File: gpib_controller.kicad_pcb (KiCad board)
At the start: 2 copper layers, 82.7 x 65.1 mm, 43 parts, among them J1 112-024-113R001, J2 FTSH-105-01-L-DV-K, J3 RJHSE5380, J4 USB4085-GF-A, U1 SN74LVC8T245PWR, U2 SN74LVC07APWR, U3 STM32H533RETx, U4 PTS645SH43SMTR92 LFS, U5 THVD1451D, U6 SN74LVC1G07DCKR, U7 SN74LVC14APWR, U8 USBLC6-2SC6, U9 TPSM861253RDXR, Y1 MU00525-32.768K, Y2 CS10820-24M

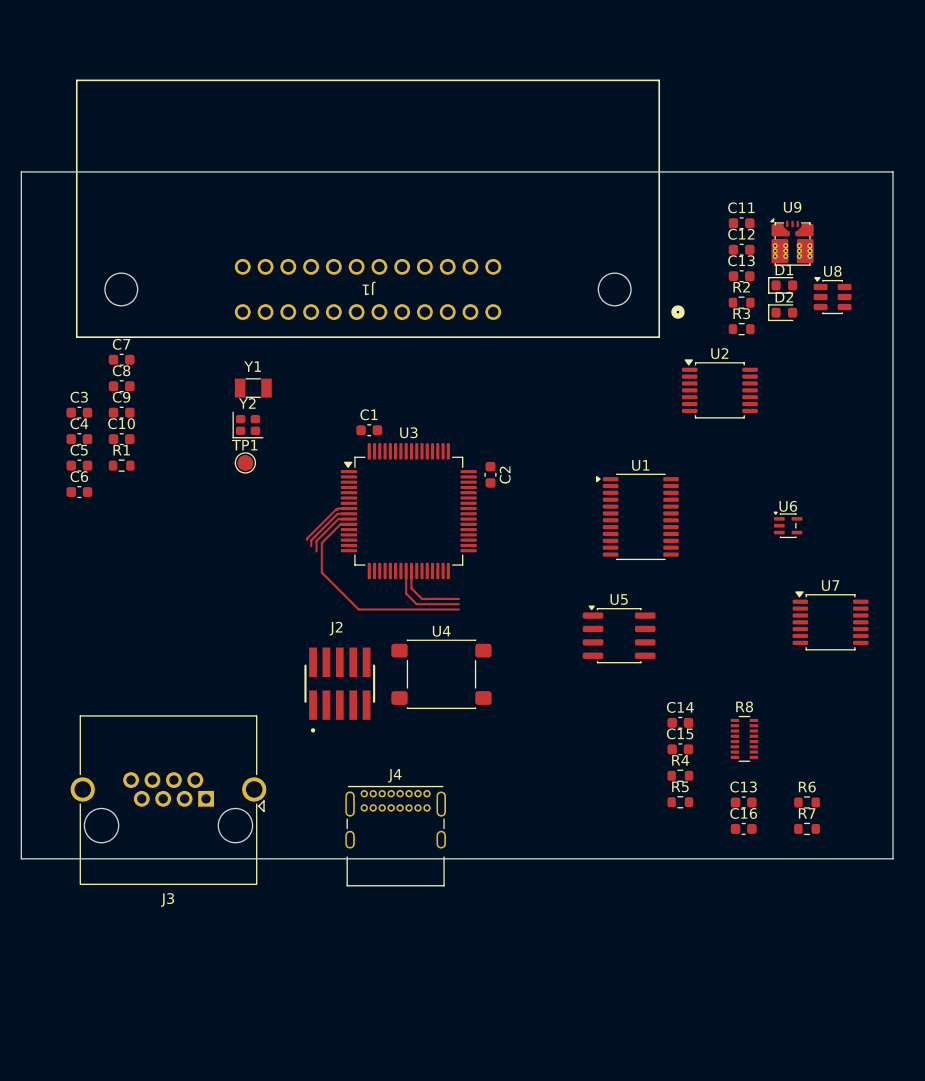
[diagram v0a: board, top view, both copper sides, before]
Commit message: Fix GPIB DIO bus nets and start PCB. Adjusted to 4 layers
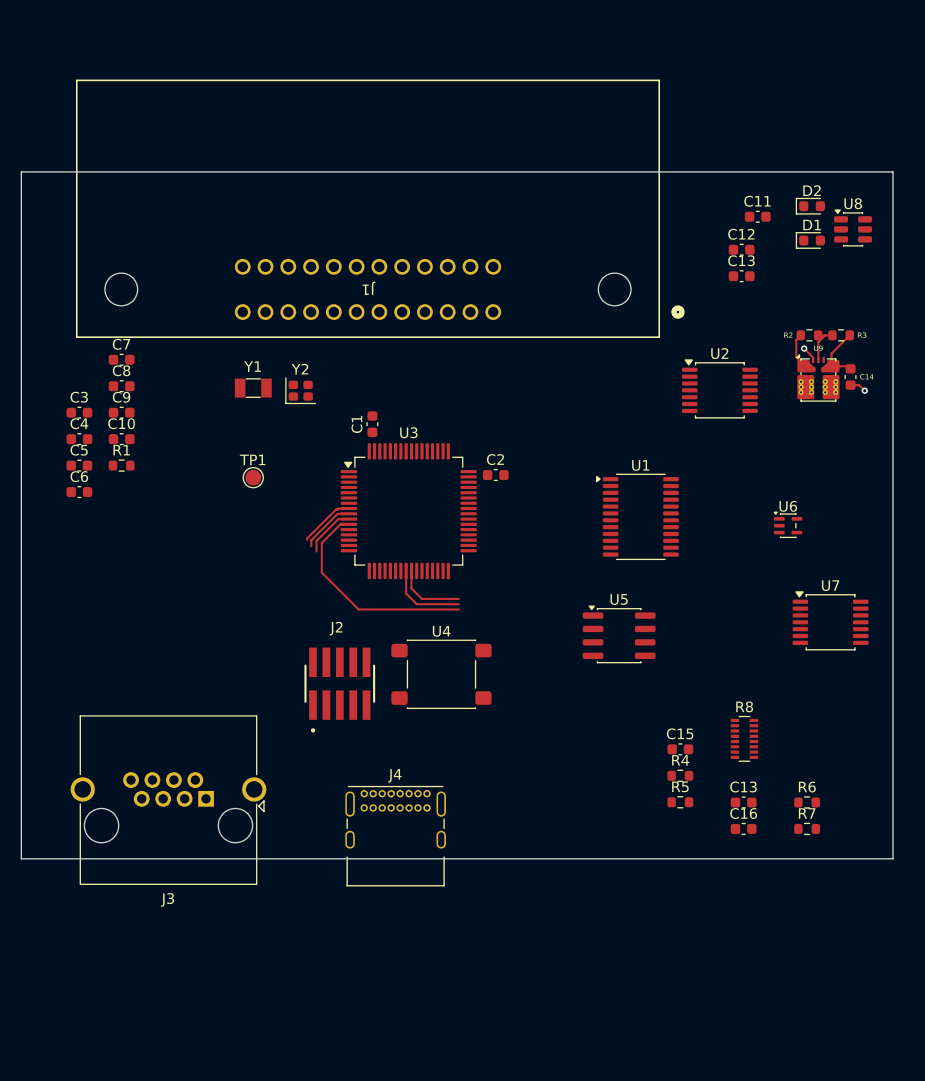
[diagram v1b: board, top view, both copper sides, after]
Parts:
- moved C14 36.6 mm to (212.2, 87.5), turned to 90 degrees
- moved U9 13.1 mm to (209.1, 87.7)
- moved D2 10.4 mm to (208.5, 71.2)
- moved R3 9.45 mm to (211.2, 83.5)
- moved R2 7.14 mm to (208.2, 83.5)
- moved U8 6.70 mm to (212.4, 73.5)
- moved Y2 5.96 mm to (160.0, 88.8)
- moved D1 5.01 mm to (208.5, 74.5)
- moved C11 1.65 mm to (203.3, 72.2)
- moved TP1 1.59 mm to (155.5, 97.0)
- moved C1 0.65 mm to (166.8, 91.9), turned to 90 degrees
- moved C2 0.50 mm to (178.5, 96.8), turned to 0 degrees
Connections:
- J1 pad 10: /Overview/Connectors/ATN -> /Overview/Connectors/SRQ
- J1 pad 17: /Overview/Connectors/ATN -> /Overview/Connectors/REN
- J1 pad 5: /Overview/Connectors/ATN -> /Overview/Connectors/EOI
- J1 pad 6: /Overview/Connectors/ATN -> /Overview/Connectors/DAV
- J1 pad 7: /Overview/Connectors/ATN -> /Overview/Connectors/NRFD
- J1 pad 8: /Overview/Connectors/ATN -> /Overview/Connectors/NDAC
- J1 pad 9: /Overview/Connectors/ATN -> /Overview/Connectors/IFC
- R8 pad 1: /Overview/Connectors/ATN -> /Overview/Connectors/DAV
- R8 pad 2: /Overview/Connectors/ATN -> /Overview/Connectors/NRFD
- R8 pad 3: /Overview/Connectors/ATN -> /Overview/Connectors/NDAC
- R8 pad 5: /Overview/Connectors/ATN -> /Overview/Connectors/IFC
- R8 pad 6: /Overview/Connectors/ATN -> /Overview/Connectors/EOI
- R8 pad 7: /Overview/Connectors/ATN -> /Overview/Connectors/REN
- R8 pad 8: /Overview/Connectors/ATN -> /Overview/Connectors/SRQ
- U1 pad 14: /Overview/GPIB Transceiver/DIO8 -> /Overview/Connectors/DIO8
- U2 pad 10: /Overview/Connectors/ATN -> /Overview/Connectors/IFC
- U2 pad 12: /Overview/Connectors/ATN -> /Overview/Connectors/EOI
- U2 pad 2: /Overview/Connectors/ATN -> /Overview/Connectors/DAV
- U2 pad 4: /Overview/Connectors/ATN -> /Overview/Connectors/NRFD
- U2 pad 6: /Overview/Connectors/ATN -> /Overview/Connectors/NDAC
- U3 pad 38: /Overview/Microcontroller/iDIO8 -> /Overview/GPIB Transceiver/iDIO8
- U6 pad 4: /Overview/Connectors/ATN -> /Overview/Connectors/REN
- U7 pad 1: /Overview/Connectors/ATN -> /Overview/Connectors/SRQ
- U7 pad 11: /Overview/Connectors/ATN -> /Overview/Connectors/DAV
- U7 pad 3: /Overview/Connectors/ATN -> /Overview/Connectors/EOI
- U7 pad 5: /Overview/Connectors/ATN -> /Overview/Connectors/NDAC
- U7 pad 9: /Overview/Connectors/ATN -> /Overview/Connectors/NRFD
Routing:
- net GND: track 0.00 -> 5.55 mm
- net Net-(U9-EN): track 0.00 -> 3.95 mm
- net +5V: track 0.00 -> 3.46 mm
- net +3V3: track 0.00 -> 3.00 mm, vias 0 -> 2
- added copper zone on In1.Cu, net +3V3
- added copper zone on In2.Cu, net GND
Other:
- copper layers 2 -> 4

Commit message: Adjust board size
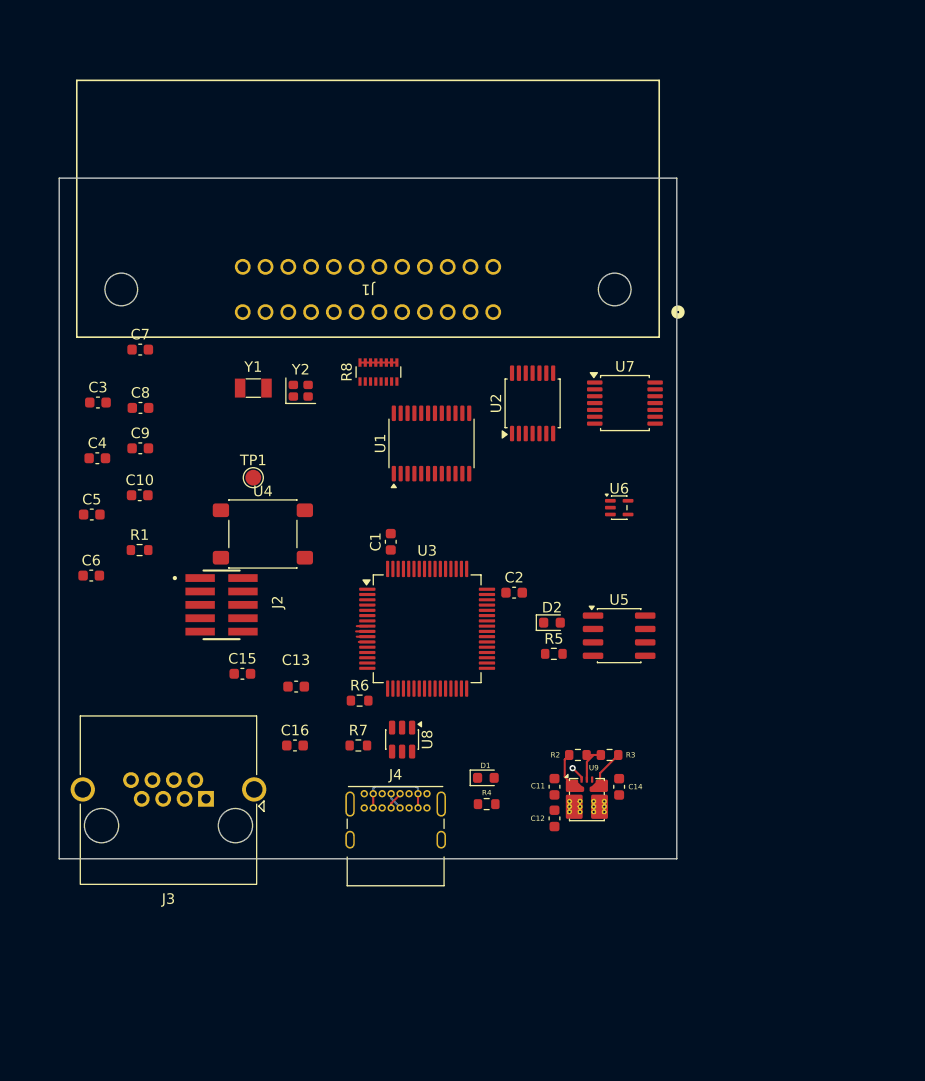
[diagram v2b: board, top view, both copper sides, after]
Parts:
- removed the C13 at (201.8, 77.9)
- moved U8 64.6 mm to (169.6, 121.8), turned to -90 degrees
- moved D1 59.6 mm to (177.6, 125.5)
- moved C11 57.4 mm to (184.1, 126.3), turned to 90 degrees
- moved C12 56.8 mm to (184.1, 129.3), turned to -90 degrees
- moved R8 49.2 mm to (167.4, 87.0), turned to 90 degrees
- moved D2 46.6 mm to (183.8, 110.8)
- moved U9 45.5 mm to (187.1, 127.5)
- moved R2 45.5 mm to (186.3, 123.3)
- moved R3 45.5 mm to (189.3, 123.3)
- moved C14 44.6 mm to (190.2, 126.3)
- moved C13 43.8 mm to (159.6, 116.8)
- moved R6 43.5 mm to (165.6, 118.1)
- moved R7 43.3 mm to (165.5, 122.4)
- moved C16 43.3 mm to (159.5, 122.4)
- moved C15 42.2 mm to (154.5, 115.6)
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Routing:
- net /Overview/GPIB Transceiver/iDIO4: track 20.6 -> 0.81 mm
- net +5V: track 3.46 -> 15.0 mm
- net /Overview/GPIB Transceiver/iDIO5: track 7.56 -> 0.00 mm
- net /Overview/GPIB Transceiver/iDIO6: track 6.56 -> 0.00 mm
- net /Overview/GPIB Transceiver/iDIO1: track 5.28 -> 1.00 mm
- net /Overview/GPIB Transceiver/iDIO2: track 5.18 -> 1.07 mm
- net /Overview/GPIB Transceiver/iDIO3: track 4.93 -> 1.00 mm
- net GND: track 5.55 -> 3.65 mm
- net /Overview/Connectors/USB_DM: track 0.00 -> 1.70 mm
- net /Overview/Connectors/USB_DP: track 0.00 -> 1.70 mm
- net +3V3: track 3.00 -> 1.44 mm, vias 2 -> 1
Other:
- board size 82.7 x 65.1 mm -> 58.6 x 64.6 mm

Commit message: Fix page numbers and finish clock layout
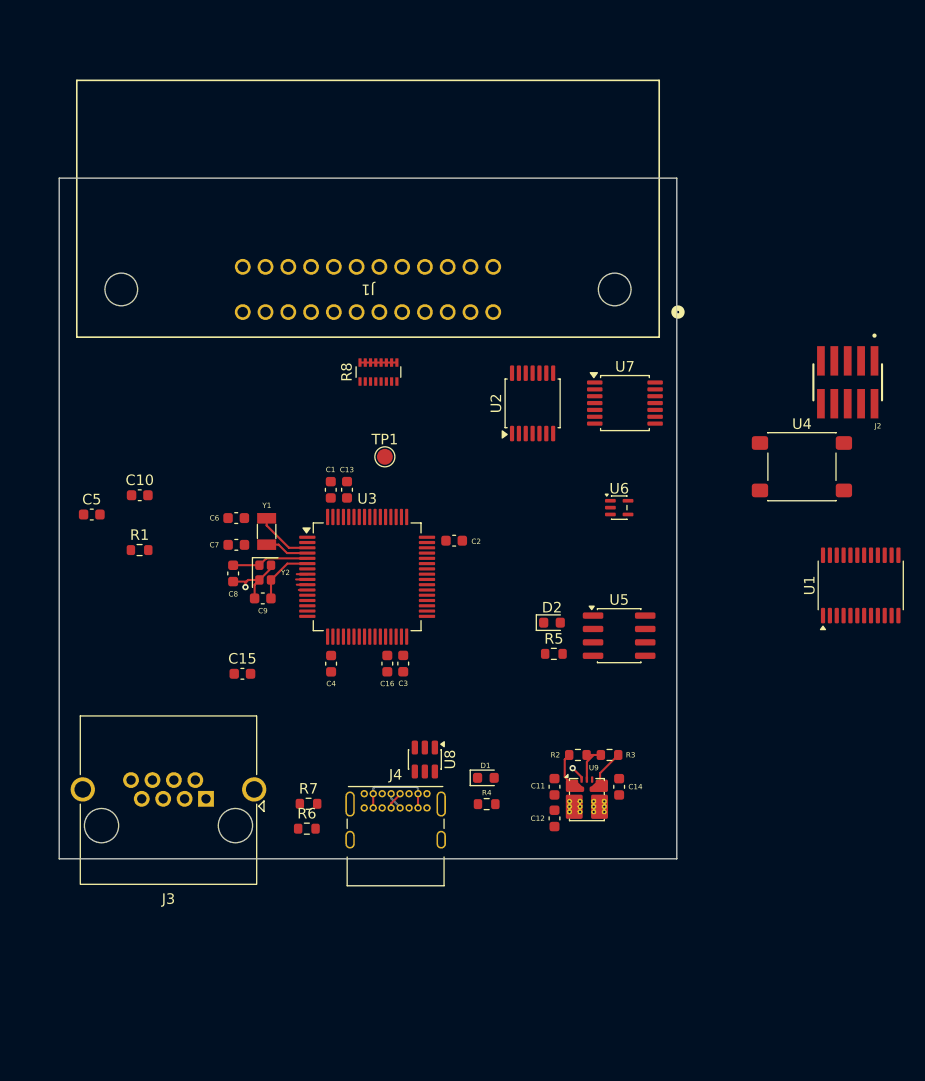
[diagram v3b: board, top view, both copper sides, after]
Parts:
- moved J2 63.0 mm to (211.9, 88.0), turned to 180 degrees
- moved U4 51.5 mm to (207.5, 96.0)
- moved U1 42.9 mm to (213.1, 107.2)
- moved C3 38.1 mm to (169.7, 114.6), turned to -90 degrees
- moved C4 29.5 mm to (162.9, 114.6), turned to -90 degrees
- moved C7 20.6 mm to (153.9, 103.4)
- moved C13 19.3 mm to (164.4, 98.1), turned to 90 degrees
- moved C9 18.4 mm to (156.4, 108.5)
- moved C8 18.0 mm to (153.6, 106.1), turned to 90 degrees
- moved Y2 17.6 mm to (156.6, 106.0), turned to -90 degrees
- moved C6 14.8 mm to (153.9, 100.8)
- moved Y1 13.7 mm to (156.8, 102.1), turned to -90 degrees
- moved R6 13.1 mm to (160.6, 130.3)
- moved TP1 12.6 mm to (168.0, 95.0)
- moved C16 11.7 mm to (168.2, 114.6), turned to -90 degrees
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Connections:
- net Net-(C13-Pad1) renamed /Overview/Microcontroller/VCAP
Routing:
- net /Overview/Microcontroller/OSC_IN: track 0.00 -> 7.31 mm
- net GND: track 3.65 -> 10.8 mm, vias 0 -> 1
- net /Overview/Microcontroller/OSC_OUT: track 0.00 -> 5.84 mm
- net /Overview/Microcontroller/OSC32_IN: track 0.00 -> 5.42 mm
- net /Overview/Microcontroller/OSC32_OUT: track 0.00 -> 4.19 mm

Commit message: Updates
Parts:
- TP1: footprint TestPoint:TestPoint_Pad_D1.5mm -> TestPoint:TestPoint_Pad_D1.0mm
- moved U5 42.7 mm to (147.6, 114.8), turned to -90 degrees
- moved U1 39.3 mm to (178.3, 89.1)
- moved U7 37.0 mm to (153.8, 88.4)
- moved C15 34.7 mm to (186.6, 102.6)
- moved R8 23.1 mm to (144.4, 88.7)
- moved U2 18.4 mm to (163.6, 88.8), turned to 180 degrees
- moved TP1 4.50 mm to (165.0, 98.4)
- moved C16 1.51 mm to (166.7, 114.6)
- moved C9 1.51 mm to (154.9, 108.4)
- moved U3 1.51 mm to (164.8, 106.4)
- moved C2 1.51 mm to (173.0, 102.9)
- moved C1 1.51 mm to (161.3, 98.1)
- moved C7 1.51 mm to (152.4, 103.3)
- moved C13 1.51 mm to (162.9, 98.1)
- moved C3 1.51 mm to (168.2, 114.6)
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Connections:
- U1 pad 10: /Overview/GPIB Transceiver/iDIO8 -> /Overview/GPIB Transceiver/iDIO5
- U1 pad 14: /Overview/Connectors/DIO8 -> /Overview/Connectors/DIO5
- U1 pad 15: /Overview/Connectors/DIO7 -> /Overview/Connectors/DIO6
- U1 pad 16: /Overview/Connectors/DIO6 -> /Overview/Connectors/DIO7
- U1 pad 17: /Overview/Connectors/DIO5 -> /Overview/Connectors/DIO8
- U1 pad 18: /Overview/Connectors/DIO4 -> /Overview/Connectors/DIO1
- U1 pad 19: /Overview/Connectors/DIO3 -> /Overview/Connectors/DIO2
- U1 pad 20: /Overview/Connectors/DIO2 -> /Overview/Connectors/DIO3
- U1 pad 21: /Overview/Connectors/DIO1 -> /Overview/Connectors/DIO4
- U1 pad 3: /Overview/GPIB Transceiver/iDIO1 -> /Overview/GPIB Transceiver/iDIO4
- U1 pad 4: /Overview/GPIB Transceiver/iDIO2 -> /Overview/GPIB Transceiver/iDIO3
- U1 pad 5: /Overview/GPIB Transceiver/iDIO3 -> /Overview/GPIB Transceiver/iDIO2
- U1 pad 6: /Overview/GPIB Transceiver/iDIO4 -> /Overview/GPIB Transceiver/iDIO1
- U1 pad 7: /Overview/GPIB Transceiver/iDIO5 -> /Overview/GPIB Transceiver/iDIO8
- U1 pad 8: /Overview/GPIB Transceiver/iDIO6 -> /Overview/GPIB Transceiver/iDIO7
- U1 pad 9: /Overview/GPIB Transceiver/iDIO7 -> /Overview/GPIB Transceiver/iDIO6
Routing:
- net GND: track 10.8 -> 28.7 mm
- net /Overview/Connectors/DIO8: track 0.00 -> 14.4 mm
- net /Overview/Connectors/DIO7: track 0.00 -> 12.7 mm
- net /Overview/Connectors/DIO6: track 0.00 -> 11.4 mm
- net /Overview/Connectors/DIO5: track 0.00 -> 10.4 mm
- net /Overview/Connectors/DAV: track 0.00 -> 8.82 mm
- net /Overview/GPIB Transceiver/iDIO4: track 0.81 -> 9.33 mm
- net +3V3: track 1.44 -> 9.28 mm
- net /Overview/GPIB Transceiver/iDIO3: track 1.00 -> 8.76 mm
- net /Overview/Connectors/NRFD: track 0.00 -> 7.38 mm
- net /Overview/Connectors/EOI: track 0.00 -> 7.38 mm
- net /Overview/Connectors/DIO4: track 0.00 -> 7.32 mm
- net /Overview/GPIB Transceiver/iDIO2: track 1.07 -> 8.11 mm
- net /Overview/Connectors/DIO3: track 0.00 -> 6.30 mm
- net /Overview/GPIB Transceiver/iDIO1: track 1.00 -> 7.29 mm
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
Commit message: Route GPIB pins
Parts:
- added H1: MountingHole, MountingHole:MountingHole_2.1mm, F.Cu at (192.4, 130.3)
- moved U2 4.76 mm to (158.8, 88.6)
- moved R8 3.56 mm to (140.8, 88.7)
- moved U7 3.42 mm to (150.4, 88.3)
- moved U1 2.98 mm to (175.5, 90.3), turned to 0 degrees
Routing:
- net /Overview/Connectors/DIO5: track 10.4 -> 20.8 mm
- net /Overview/Connectors/DIO6: track 11.4 -> 21.2 mm
- net /Overview/Connectors/DIO7: track 12.7 -> 21.7 mm
- net /Overview/Connectors/DAV: track 8.82 -> 0.00 mm
- net /Overview/Connectors/DIO8: track 14.4 -> 22.6 mm
- net /Overview/Connectors/DIO3: track 6.30 -> 14.4 mm
- net /Overview/Connectors/DIO1: track 5.05 -> 13.1 mm
- net /Overview/Connectors/DIO4: track 7.32 -> 15.3 mm
- net /Overview/Connectors/DIO2: track 5.68 -> 13.5 mm
- net /Overview/Connectors/NRFD: track 7.38 -> 0.00 mm
- net /Overview/Connectors/EOI: track 7.38 -> 0.00 mm
- net /Overview/Connectors/IFC: track 6.24 -> 0.00 mm
- net /Overview/Connectors/NDAC: track 5.90 -> 0.00 mm
- net /Overview/Connectors/ATN: track 4.34 -> 0.00 mm
